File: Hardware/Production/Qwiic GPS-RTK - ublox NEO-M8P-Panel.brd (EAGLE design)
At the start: 95.5 x 94.2 mm, 406 parts, among them J11 PTH, J13 U.FL, J15 U.FL, J17 PTH, J20 U.FL, J3 PTH, J5 PTH, J9 U.FL, U1 NEO-M8P, U2 3.3V, U3 NEO-M8P, U4 3.3V, U5 NEO-M8P, U6 3.3V, U7 NEO-M8P, U8 3.3V

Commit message: Adding examples
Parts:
- removed JP52: (no value), SparkFun-Jumpers:SMT-JUMPER_2_NO_SILK
- removed JP53, JP54: (no value), SparkFun-Jumpers:SMT-JUMPER_2_NC_TRACE_SILK
- removed JP55: SPI, SparkFun-Connectors:1X06_NO_SILK
- added J21: (no value), SparkFun-Connectors:1X04_1MM_RA
- added J22: (no value), SparkFun-Connectors:USB-MICROB-PTH-MILL
- added J23: U.FL, SparkFun-Connectors:U.FL
- added J24: (no value), SparkFun-Connectors:1X07_NO_SILK
- added U$197, U$198: (no value), Labels:CS#-<]
- added U$199, U$200: (no value), Labels:MISO-(]-04
- added U$201, U$202: (no value), Labels:MOSI-(]-04
- added U$203, U$204: (no value), Labels:SCK-(]-04
- J1, J18: device SparkFun-Connectors:1X04_1MM_RA -> SparkFun-Connectors:1X07_NO_SILK
- J10: value (none) -> U.FL; device SparkFun-Connectors:1X04_1MM_RA -> SparkFun-Connectors:U.FL
- J11: value PTH -> (none); device SparkX:1X04_NO_SILK -> SparkFun-Connectors:1X07_NO_SILK
- J14: value (none) -> PTH; device SparkFun-Connectors:USB-MICROB-PTH-MILL -> SparkX:1X04_NO_SILK
- J15: value U.FL -> (none); device SparkFun-Connectors:U.FL -> SparkFun-Connectors:1X04_1MM_RA
- J16: device SparkFun-Connectors:1X04_1MM_RA -> SparkFun-Connectors:USB-MICROB-PTH-MILL
- J17: value PTH -> U.FL; device SparkX:1X04_NO_SILK -> SparkFun-Connectors:U.FL
- J19, J8: device SparkFun-Connectors:USB-MICROB-PTH-MILL -> SparkFun-Connectors:1X04_1MM_RA
- J20: value U.FL -> PTH; device SparkFun-Connectors:U.FL -> SparkX:1X04_NO_SILK
- J5: value PTH -> (none); device SparkX:1X04_NO_SILK -> SparkFun-Connectors:1X04_1MM_RA
- J7: value (none) -> PTH; device SparkFun-Connectors:1X04_1MM_RA -> SparkX:1X04_NO_SILK
- J9: value U.FL -> (none); device SparkFun-Connectors:U.FL -> SparkFun-Connectors:USB-MICROB-PTH-MILL
- JP11, JP38: value SPI -> FIDUCIALUFIDUCIAL; device SparkFun-Connectors:1X06_NO_SILK -> SparkFun:MICRO-FIDUCIAL
- JP13, JP29, JP30, JP46: value FIDUCIALUFIDUCIAL -> STAND-OFF; device SparkFun:MICRO-FIDUCIAL -> SparkFun:STAND-OFF
- JP16, JP32: value STAND-OFF -> (none); device SparkFun:STAND-OFF -> SparkFun-Jumpers:SMT-JUMPER_2_NO_SILK
- JP17, JP34: value SPI -> (none); device SparkFun-Connectors:1X06_NO_SILK -> SparkFun-Jumpers:SMT-JUMPER_2_NC_TRACE_SILK
- JP18: device SparkFun-Jumpers:SMT-JUMPER_2_NO_SILK -> SparkFun-Jumpers:SMT-JUMPER_2_NC_TRACE_SILK
- JP19: value (none) -> SPI; device SparkFun-Jumpers:SMT-JUMPER_2_NC_TRACE_SILK -> SparkFun-Connectors:1X06_NO_SILK
- JP20, JP36, JP37, JP45: value (none) -> STAND-OFF; device SparkFun-Jumpers:SMT-JUMPER_2_NC_TRACE_SILK -> SparkFun:STAND-OFF
- JP22: value SPI -> STAND-OFF; device SparkFun-Connectors:1X06_NO_SILK -> SparkFun:STAND-OFF
- JP23, JP24, JP39: value STAND-OFF -> FIDUCIALUFIDUCIAL; device SparkFun:STAND-OFF -> SparkFun:MICRO-FIDUCIAL
- JP25: value FIDUCIALUFIDUCIAL -> (none); device SparkFun:MICRO-FIDUCIAL -> SparkFun-Jumpers:SMT-JUMPER_3_2-NC_TRACE_SILK
- JP26, JP42: value FIDUCIALUFIDUCIAL -> (none); device SparkFun:MICRO-FIDUCIAL -> SparkFun-Jumpers:SMT-JUMPER_2_NC_TRACE_SILK
- JP27, JP44: value (none) -> FIDUCIALUFIDUCIAL; device SparkFun-Jumpers:SMT-JUMPER_3_2-NC_TRACE_SILK -> SparkFun:MICRO-FIDUCIAL
- JP28: value (none) -> FIDUCIALUFIDUCIAL; device SparkFun-Jumpers:SMT-JUMPER_2_NC_TRACE_SILK -> SparkFun:MICRO-FIDUCIAL
- JP33, JP48, JP49: value STAND-OFF -> (none); device SparkFun:STAND-OFF -> SparkFun-Jumpers:SMT-JUMPER_2_NC_TRACE_SILK
- JP35: value (none) -> SPI; device SparkFun-Jumpers:SMT-JUMPER_2_NO_SILK -> SparkFun-Connectors:1X06_NO_SILK
- JP40: value STAND-OFF -> (none); device SparkFun:STAND-OFF -> SparkFun-Jumpers:SMT-JUMPER_3_2-NC_TRACE_SILK
- JP47: value FIDUCIALUFIDUCIAL -> (none); device SparkFun:MICRO-FIDUCIAL -> SparkFun-Jumpers:SMT-JUMPER_2_NO_SILK
- R10, R25, R26, R40, R41, R55, R56, R9: value 33 -> 27
- U$100, U$151: device Labels:SCL-[) -> Labels:MOSI-(]-04
- U$101: device Labels:SDA-[) -> Labels:SCK-(]-04
- U$102: device Labels:SCL-[) -> Labels:SCK-(]-04
- U$103: device Labels:3V3-04 -> Labels:SDA-[)
- U$104: device Labels:3V3-04 -> Labels:SCL-[)
- U$105, U$154: device Labels:GND-04 -> Labels:SDA-[)
- U$106, U$155: device Labels:GND-04 -> Labels:SCL-[)
- U$107: device Labels:I_SUPER2_C-()-03 -> Labels:3V3-04
- U$108, U$158: device buzzard_labels (5):INT8 -> Labels:3V3-04
- U$109, U$51: device buzzard_labels (5):INT8 -> Labels:GND-04
- U$110: device buzzard_labels (5):U#BLOX3 -> Labels:GND-04
- U$111: device Labels:QWIIC-LOGO-MEDIUM -> Labels:I_SUPER2_C-()-03
- U$112, U$58: value SPARKX-LOGO3 -> (none); device SparkX:SPARKX-SMALL -> buzzard_labels (5):INT8
- U$113: value SPARKX-LOGO4 -> (none); device SparkX:SPARKX-MEDIUM -> buzzard_labels (5):INT8
- U$114: device buzzard_labels (7):#RST3 -> buzzard_labels (5):U#BLOX3
- U$115: device buzzard_labels (7):#RST3 -> Labels:QWIIC-LOGO-MEDIUM
- U$116: value (none) -> SPARKX-LOGO3; device buzzard_labels (7):#SAFE1 -> SparkX:SPARKX-SMALL
- U$117: value (none) -> SPARKX-LOGO4; device buzzard_labels (7):#SAFE1 -> SparkX:SPARKX-MEDIUM
- U$118, U$119: device buzzard_labels (7):PPS5 -> buzzard_labels (7):#RST3
- U$120: device buzzard_labels (33):PPS0 -> buzzard_labels (7):#SAFE1
- U$121: device buzzard_labels:FENCE2 -> buzzard_labels (7):#SAFE1
- U$122: device buzzard_labels:JP20 -> buzzard_labels (7):PPS5
- U$123: device buzzard_labels:RTK1 -> buzzard_labels (7):PPS5
- U$124: device buzzard_labels (1):FENCE0 -> buzzard_labels (33):PPS0
- U$125: device buzzard_labels (1):FENCE0 -> buzzard_labels:FENCE2
- U$126: device buzzard_labels (1):RTK1 -> buzzard_labels:JP20
- U$127: device buzzard_labels (1):RTK1 -> buzzard_labels:RTK1
- U$128, U$129: device Labels:MISO -> buzzard_labels (1):FENCE0
- U$130, U$131: device Labels:MOSI -> buzzard_labels (1):RTK1
- U$132, U$133, U$48, U$49: device Labels:SCK-[) -> Labels:3V3-04
- U$134, U$135, U$50: device Labels:CS#-[> -> Labels:GND-04
- U$136: device Labels:3V3-04 -> buzzard_labels (3):GPS#RTK0
- U$137: device Labels:3V3-04 -> buzzard_labels (5):JP10
- U$138: device Labels:GND-04 -> buzzard_labels (5):JP32
- U$139: device Labels:GND-04 -> buzzard_labels (6):DSEL0
- U$140: device buzzard_labels (3):GPS#RTK0 -> buzzard_labels (7):NEO#M8P3
- U$141: device buzzard_labels (5):JP10 -> buzzard_labels (8):GPS#RTK1
- U$142: device buzzard_labels (5):JP32 -> buzzard_labels (9):ANT0
- U$143: device buzzard_labels (6):DSEL0 -> Labels:PWR-()-03
- U$144: device buzzard_labels (7):NEO#M8P3 -> Labels:5V
- U$145: device buzzard_labels (8):GPS#RTK1 -> Labels:5V
- U$146: device buzzard_labels (9):ANT0 -> Labels:CS#-<]
- U$147: device Labels:PWR-()-03 -> Labels:CS#-<]
- U$148: device Labels:SDA-[) -> Labels:MISO-(]-04
- U$149: device Labels:SCL-[) -> Labels:MISO-(]-04
- U$150, U$99: device Labels:SDA-[) -> Labels:MOSI-(]-04
- U$152, U$153: device Labels:3V3-04 -> Labels:SCK-(]-04
- U$156: device Labels:I_SUPER2_C-()-03 -> Labels:SDA-[)
- U$157: device buzzard_labels (5):INT8 -> Labels:SCL-[)
- U$159: device buzzard_labels (5):U#BLOX3 -> Labels:3V3-04
- U$160: device Labels:QWIIC-LOGO-MEDIUM -> Labels:GND-04
- U$161: value SPARKX-LOGO3 -> (none); device SparkX:SPARKX-SMALL -> Labels:GND-04
- U$162: value SPARKX-LOGO4 -> (none); device SparkX:SPARKX-MEDIUM -> Labels:I_SUPER2_C-()-03
- U$163, U$164: device buzzard_labels (7):#RST3 -> buzzard_labels (5):INT8
- U$165: device buzzard_labels (7):#SAFE1 -> buzzard_labels (5):U#BLOX3
- U$166: device buzzard_labels (7):#SAFE1 -> Labels:QWIIC-LOGO-MEDIUM
- U$167: value (none) -> SPARKX-LOGO3; device buzzard_labels (7):PPS5 -> SparkX:SPARKX-SMALL
- U$168: value (none) -> SPARKX-LOGO4; device buzzard_labels (7):PPS5 -> SparkX:SPARKX-MEDIUM
- U$169: device buzzard_labels (33):PPS0 -> buzzard_labels (7):#RST3
- U$170: device buzzard_labels:FENCE2 -> buzzard_labels (7):#RST3
- U$171: device buzzard_labels:JP20 -> buzzard_labels (7):#SAFE1
- U$172: device buzzard_labels:RTK1 -> buzzard_labels (7):#SAFE1
- U$173, U$174: device buzzard_labels (1):FENCE0 -> buzzard_labels (7):PPS5
- U$175: device buzzard_labels (1):RTK1 -> buzzard_labels (33):PPS0
- U$176: device buzzard_labels (1):RTK1 -> buzzard_labels:FENCE2
- U$177: device Labels:MISO -> buzzard_labels:JP20
- U$178: device Labels:MISO -> buzzard_labels:RTK1
- U$179, U$180: device Labels:MOSI -> buzzard_labels (1):FENCE0
- U$181, U$182: device Labels:SCK-[) -> buzzard_labels (1):RTK1
- U$183, U$184: device Labels:CS#-[> -> Labels:3V3-04
- U$185, U$186: device Labels:3V3-04 -> Labels:GND-04
- U$187: device Labels:GND-04 -> buzzard_labels (3):GPS#RTK0
- U$188: device Labels:GND-04 -> buzzard_labels (5):JP10
- U$189: device buzzard_labels (3):GPS#RTK0 -> buzzard_labels (5):JP32
- U$19: device Labels:SDA-[) -> Labels:5V
- U$190: device buzzard_labels (5):JP10 -> buzzard_labels (6):DSEL0
- U$191: device buzzard_labels (5):JP32 -> buzzard_labels (7):NEO#M8P3
- U$192: device buzzard_labels (6):DSEL0 -> buzzard_labels (8):GPS#RTK1
- U$193: device buzzard_labels (7):NEO#M8P3 -> buzzard_labels (9):ANT0
- U$194: device buzzard_labels (8):GPS#RTK1 -> Labels:PWR-()-03
- U$195: device buzzard_labels (9):ANT0 -> Labels:5V
- U$196: device Labels:PWR-()-03 -> Labels:5V
- U$20: device Labels:SCL-[) -> Labels:5V
- U$23: device Labels:SDA-[) -> Labels:CS#-<]
- U$24: device Labels:SCL-[) -> Labels:CS#-<]
- U$26, U$33: device Labels:3V3-04 -> Labels:MISO-(]-04
- U$34, U$37: device Labels:GND-04 -> Labels:MOSI-(]-04
- U$38: device Labels:I_SUPER2_C-()-03 -> Labels:SCK-(]-04
- U$41: device buzzard_labels (5):INT8 -> Labels:SCK-(]-04
- U$42: device Labels:MISO -> Labels:SDA-[)
- U$45: device Labels:MISO -> Labels:SCL-[)
- U$46: device Labels:MOSI -> Labels:SDA-[)
- U$47: device Labels:MOSI -> Labels:SCL-[)
- U$56: device buzzard_labels (5):U#BLOX3 -> Labels:I_SUPER2_C-()-03
- U$57: device Labels:QWIIC-LOGO-MEDIUM -> buzzard_labels (5):INT8
- U$59: device Labels:CS#-[> -> buzzard_labels (5):U#BLOX3
- U$64: value SPARKX-LOGO4 -> (none); device SparkX:SPARKX-MEDIUM -> Labels:QWIIC-LOGO-MEDIUM
- U$65: value (none) -> SPARKX-LOGO3; device buzzard_labels (7):#RST3 -> SparkX:SPARKX-SMALL
- U$66: value (none) -> SPARKX-LOGO4; device buzzard_labels (7):#RST3 -> SparkX:SPARKX-MEDIUM
- U$67, U$68: device buzzard_labels (7):#SAFE1 -> buzzard_labels (7):#RST3
- U$69, U$70: device buzzard_labels (7):PPS5 -> buzzard_labels (7):#SAFE1
- U$71: device buzzard_labels (33):PPS0 -> buzzard_labels (7):PPS5
- U$72: device buzzard_labels:FENCE2 -> buzzard_labels (7):PPS5
- U$73: device buzzard_labels:JP20 -> buzzard_labels (33):PPS0
- U$74: device buzzard_labels:RTK1 -> buzzard_labels:FENCE2
- U$75: device buzzard_labels (1):FENCE0 -> buzzard_labels:JP20
- U$76: device buzzard_labels (1):FENCE0 -> buzzard_labels:RTK1
- U$77, U$78: device buzzard_labels (1):RTK1 -> buzzard_labels (1):FENCE0
- U$79, U$80: device Labels:MISO -> buzzard_labels (1):RTK1
- U$81, U$82: device Labels:MOSI -> Labels:3V3-04
- U$83, U$84: device Labels:SCK-[) -> Labels:GND-04
- U$85: device Labels:CS#-[> -> buzzard_labels (3):GPS#RTK0
- U$86: device Labels:CS#-[> -> buzzard_labels (5):JP10
- U$87: device Labels:3V3-04 -> buzzard_labels (5):JP32
- U$88: device Labels:3V3-04 -> buzzard_labels (6):DSEL0
- U$89: device Labels:GND-04 -> buzzard_labels (7):NEO#M8P3
- U$90: device Labels:GND-04 -> buzzard_labels (8):GPS#RTK1
- U$91: device buzzard_labels (3):GPS#RTK0 -> buzzard_labels (9):ANT0
- U$92: device buzzard_labels (5):JP10 -> Labels:PWR-()-03
- U$93: device buzzard_labels (5):JP32 -> Labels:5V
- U$94: device buzzard_labels (6):DSEL0 -> Labels:5V
- U$95: device buzzard_labels (7):NEO#M8P3 -> Labels:CS#-<]
- U$96: device buzzard_labels (8):GPS#RTK1 -> Labels:CS#-<]
- U$97: device buzzard_labels (9):ANT0 -> Labels:MISO-(]-04
- U$98: device Labels:PWR-()-03 -> Labels:MISO-(]-04
- moved JP20 95.5 mm to (2.54, 66.5), flipped to the top
- moved J10 73.9 mm to (72.5, 22.4), turned to 180 degrees
- moved JP22 69.8 mm to (38.1, 66.5), turned to 0 degrees
- moved JP11 67.2 mm to (81.2, 0.64), flipped to the bottom
- moved J18 59.6 mm to (19.1, 67.8), turned to 0 degrees
- moved JP38 59.6 mm to (81.2, 36.7), turned to 0 degrees
- moved U$20 57.5 mm to (21.6, 27.7), flipped to the bottom
- moved U$19 55.3 mm to (21.6, 27.7)
- moved U$24 53.2 mm to (26.7, 27.9)
- moved U$47 52.9 mm to (72.9, 1.65), flipped to the bottom, turned to 90 degrees
- moved U$23 51.0 mm to (26.7, 27.9), flipped to the top
- moved U$46 50.8 mm to (70.4, 1.65), turned to 90 degrees
- moved U$45 50.8 mm to (72.9, 1.65), flipped to the top, turned to 90 degrees
- moved JP12 50.6 mm to (41.8, 32.4)
- moved JP43 50.6 mm to (81.2, 36.7), flipped to the bottom
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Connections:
- net !RESET1: now also JP19.3; no longer JP22.3
- net !RESET2: now also JP35.3; no longer JP38.3
- net !RESET3: now also JP50.3; no longer JP55.3
- net !SAFE1: now also JP19.2; no longer JP22.2
- net !SAFE2: now also JP35.2; no longer JP38.2
- net !SAFE3: now also JP50.2; no longer JP55.2
- net 3.3V: now also J1.3; no longer JP11.2
- net 3.3V1: now also J11.3, J8.2; no longer J1.2, JP17.2
- net 3.3V2: now also J14.2, J15.2, J18.3, JP25.2; no longer J10.2, J11.2, JP27.2, JP34.2
- net 3.3V3: now also J19.2, J20.2, J21.2, J24.3, JP40.2; no longer J16.2, J17.2, J18.2, JP44.2, JP50.2
- net 5V: now also J1.2
- net 5V1: now also J11.2, J9.VBUS; no longer J8.VBUS
- net 5V2: now also J16.VBUS, J18.2; no longer J14.VBUS
- net 5V3: now also J22.VBUS, J24.2; no longer J19.VBUS
- net D_SEL1: now also JP16.2; no longer JP18.2
- net D_SEL2: now also JP32.2; no longer JP35.2
- net D_SEL3: now also JP47.2; no longer JP52.2
- net FENCE_STAT1: now also JP18.2, JP19.6; no longer JP20.2, JP22.6
- net FENCE_STAT2: now also JP34.2, JP35.6; no longer JP37.2, JP38.6
- net FENCE_STAT3: now also JP49.2, JP50.6; no longer JP54.2, JP55.6
- net GND: now also J1.1; no longer JP11.1
- net GND1: now also J10.1, J10.2, J11.1, J8.1, J9.GND, JP16.1; no longer J1.1, J8.GND, J9.1, J9.2, JP17.1, JP18.1
- net GND2: now also J14.1, J16.GND, J17.1, J17.2, J18.1, JP32.1; no longer J10.1, J11.1, J14.GND, J15.2, JP34.1, JP35.1
- net GND3: now also J19.1, J21.1, J22.GND, J23.1, J23.2, J24.1, JP47.1; no longer J16.1, J17.1, J18.1, J19.GND, J20.2, JP50.1, JP52.1
- net GPS_ANT2: now also J10.FEED; no longer J9.FEED
- net GPS_ANT3: now also J17.FEED; no longer J15.FEED
- net GPS_ANT4: now also J23.FEED; no longer J20.FEED
- net INT1: now also JP19.1; no longer JP22.1
- net INT2: now also JP35.1; no longer JP38.1
- net INT3: now also JP50.1; no longer JP55.1
- net N$23: now also JP17.1; no longer JP19.1
- net N$25: now also JP18.1; no longer JP20.1
- net N$27: now also JP25.1; no longer JP27.1
- net N$28: now also JP25.3; no longer JP27.3
- net N$30: now also JP26.1; no longer JP28.1
- net N$36: now also JP33.1; no longer JP36.1
- net N$38: now also JP34.1; no longer JP37.1
- net N$40: now also JP40.1; no longer JP44.1
- net N$41: now also JP40.3; no longer JP44.3
- net N$43: now also JP42.1; no longer JP45.1
- net N$49: now also JP48.1; no longer JP53.1
- net N$51: now also JP49.1; no longer JP54.1
- net PPS1: now also JP19.4; no longer JP22.4
- net PPS2: now also JP26.2, JP35.4; no longer JP28.2, JP38.4
- net PPS3: now also JP42.2, JP50.4; no longer JP45.2, JP55.4
- net RTK_STAT1: now also JP17.2, JP19.5; no longer JP19.2, JP22.5
- net RTK_STAT2: now also JP33.2, JP35.5; no longer JP36.2, JP38.5
- net RTK_STAT3: now also JP48.2, JP50.5; no longer JP53.2, JP55.5
- net RXI/MOSI: now also J1.5; no longer JP11.4
- net RXI/MOSI1: now also J11.5; no longer JP17.4
- net RXI/MOSI2: now also J18.5; no longer JP34.4
- net RXI/MOSI3: now also J24.5; no longer JP50.4
- net SCL/SCK: now also J1.7; no longer JP11.6
- net SCL/SCK1: now also J11.7, J8.4; no longer J1.4, JP17.6
- net SCL/SCK2: now also J14.4, J15.4, J18.7; no longer J10.4, J11.4, JP34.6
- net SCL/SCK3: now also J19.4, J20.4, J21.4, J24.7; no longer J16.4, J17.4, J18.4, JP50.6
- net SDA/!CS: now also J1.4; no longer JP11.3
- net SDA/!CS1: now also J11.4, J8.3; no longer J1.3, JP17.3
- net SDA/!CS2: now also J14.3, J15.3, J18.4; no longer J10.3, J11.3, JP34.3
- net SDA/!CS3: now also J19.3, J20.3, J21.3, J24.4; no longer J16.3, J17.3, J18.3, JP50.3
- net SHLD1: now also J9.SHIELD, J9.SHIELD10, J9.SHIELD2, J9.SHIELD3, J9.SHIELD4, J9.SHIELD5, J9.SHIELD6, J9.SHIELD7, J9.SHIELD8, J9.SHIELD9; no longer J8.SHIELD, J8.SHIELD10, J8.SHIELD2, J8.SHIELD3, J8.SHIELD4, J8.SHIELD5, J8.SHIELD6, J8.SHIELD7, J8.SHIELD8, J8.SHIELD9
- net SHLD2: now also J16.SHIELD, J16.SHIELD10, J16.SHIELD2, J16.SHIELD3, J16.SHIELD4, J16.SHIELD5, J16.SHIELD6, J16.SHIELD7, J16.SHIELD8, J16.SHIELD9; no longer J14.SHIELD, J14.SHIELD10, J14.SHIELD2, J14.SHIELD3, J14.SHIELD4, J14.SHIELD5, J14.SHIELD6, J14.SHIELD7, J14.SHIELD8, J14.SHIELD9
- net SHLD3: now also J22.SHIELD, J22.SHIELD10, J22.SHIELD2, J22.SHIELD3, J22.SHIELD4, J22.SHIELD5, J22.SHIELD6, J22.SHIELD7, J22.SHIELD8, J22.SHIELD9; no longer J19.SHIELD, J19.SHIELD10, J19.SHIELD2, J19.SHIELD3, J19.SHIELD4, J19.SHIELD5, J19.SHIELD6, J19.SHIELD7, J19.SHIELD8, J19.SHIELD9
- net TXO/MISO: now also J1.6; no longer JP11.5
- net TXO/MISO1: now also J11.6; no longer JP17.5
- net TXO/MISO2: now also J18.6; no longer JP34.5
- net TXO/MISO3: now also J24.6; no longer JP50.5
- net USB_D+1: now also J9.D+; no longer J8.D+
- net USB_D+2: now also J16.D+; no longer J14.D+
- net USB_D+3: now also J22.D+; no longer J19.D+
- net USB_D-1: now also J9.D-; no longer J8.D-
- net USB_D-2: now also J16.D-; no longer J14.D-
- net USB_D-3: now also J22.D-; no longer J19.D-
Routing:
- net 5V3: track 21.3 -> 53.6 mm
- net 5V: track 21.3 -> 53.6 mm
- net 5V2: track 21.3 -> 53.6 mm
- net 5V1: track 21.3 -> 53.6 mm
- net N$33: track 25.6 -> 55.8 mm
- net N$46: track 25.6 -> 55.8 mm
- net N$11: track 25.6 -> 55.8 mm
- net N$20: track 25.6 -> 55.8 mm
- net N$34: track 24.4 -> 52.4 mm
- net N$12: track 24.4 -> 52.4 mm
- net N$47: track 24.4 -> 52.4 mm
- net N$21: track 24.4 -> 52.4 mm
- net INT2: track 15.5 -> 24.0 mm
- net INT: track 15.5 -> 24.0 mm
- net INT1: track 15.5 -> 24.0 mm
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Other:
- board text added: "x02"
- board text removed: "x01"

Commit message: Modifications for reds.
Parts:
- removed E$4: (no value), SparkFun-Aesthetics:FIDUCIAL-1X2
- removed E$5, E$6: (no value), SparkFun-Retired:FIDUCIAL-1.5X3
- removed U$201, U$202: (no value), Labels:MOSI-(]-04
- removed U$203, U$204: (no value), Labels:SCK-(]-04
- added LOGO5, LOGO7: OSHW-LOGOMINI, SparkFun-Aesthetics:OSHW-LOGO-MINI
- added LOGO6, LOGO8: SFE_LOGO_NAME_FLAME.1_INCH, SparkFun-Aesthetics:SFE_LOGO_NAME_FLAME_.1
- D1, D11, D16, D6: value BLUE -> Yellow
- E$3: device SparkFun-Aesthetics:FIDUCIAL-1X2 -> SparkFun-Retired:FIDUCIAL-1.5X3
- JP10, JP26, JP42: device SparkFun-Jumpers:SMT-JUMPER_2_NC_TRACE_SILK -> SparkFun-Jumpers:SMT-JUMPER_3_2-NC_TRACE_SILK
- JP11, JP27, JP43: value FIDUCIALUFIDUCIAL -> (none); device SparkFun:MICRO-FIDUCIAL -> SparkFun-Jumpers:SMT-JUMPER_2_NC_TRACE_SILK
- JP13, JP29, JP45: value STAND-OFF -> FIDUCIALUFIDUCIAL; device SparkFun:STAND-OFF -> SparkFun:MICRO-FIDUCIAL
- JP15: value SPI -> (none)
- JP16, JP32, JP47: value (none) -> STAND-OFF; device SparkFun-Jumpers:SMT-JUMPER_2_NO_SILK -> SparkFun:STAND-OFF
- JP17, JP33, JP48: device SparkFun-Jumpers:SMT-JUMPER_2_NC_TRACE_SILK -> SparkFun-Jumpers:SMT-JUMPER_2_NO_SILK
- JP19, JP35, JP50: value SPI -> (none); device SparkFun-Connectors:1X06_NO_SILK -> SparkFun-Jumpers:SMT-JUMPER_2_NC_TRACE_SILK
- JP20, JP36: value STAND-OFF -> (none); device SparkFun:STAND-OFF -> SparkFun-Connectors:1X06_NO_SILK
- JP23, JP38, JP7: value FIDUCIALUFIDUCIAL -> STAND-OFF; device SparkFun:MICRO-FIDUCIAL -> SparkFun:STAND-OFF
- JP25, JP40, JP9: value (none) -> FIDUCIALUFIDUCIAL; device SparkFun-Jumpers:SMT-JUMPER_3_2-NC_TRACE_SILK -> SparkFun:MICRO-FIDUCIAL
- JP5: value STAND-OFF -> (none); device SparkFun:STAND-OFF -> SparkFun-Jumpers:SMT-JUMPER_3_2-NC_TRACE_SILK
- JP51: device SparkFun-Jumpers:SMT-JUMPER_3_2-NC_TRACE_SILK -> SparkFun-Connectors:1X06_NO_SILK
- LOGO2, LOGO4: value OSHW-LOGOMINI -> SFE_LOGO_NAME_FLAME.1_INCH; device SparkFun-Aesthetics:OSHW-LOGO-MINI -> SparkFun-Aesthetics:SFE_LOGO_NAME_FLAME_.1
- U$100, U$150, U$37: device Labels:MOSI-(]-04 -> buzzard_labels (36):TX#MISO1
- U$101, U$153: device Labels:SCK-(]-04 -> Labels:SDA-[)
- U$102, U$152: device Labels:SCK-(]-04 -> Labels:SCL-[)
- U$105, U$156: device Labels:SDA-[) -> Labels:3V3-04
- U$106, U$155, U$47: device Labels:SCL-[) -> Labels:3V3-04
- U$107, U$108, U$158, U$49, U$81: device Labels:3V3-04 -> Labels:GND-04
- U$109, U$51: device Labels:GND-04 -> Labels:I_SUPER2_C-()-03
- U$110, U$160, U$161: device Labels:GND-04 -> buzzard_labels (5):INT8
- U$111, U$56: device Labels:I_SUPER2_C-()-03 -> buzzard_labels (5):INT8
- U$112, U$58: device buzzard_labels (5):INT8 -> buzzard_labels (5):U#BLOX3
- U$113, U$163: device buzzard_labels (5):INT8 -> Labels:QWIIC-LOGO-MEDIUM
- U$114, U$165: device buzzard_labels (5):U#BLOX3 -> buzzard_labels (7):#RST3
- U$115, U$64: device Labels:QWIIC-LOGO-MEDIUM -> buzzard_labels (7):#RST3
- U$116, U$167: value SPARKX-LOGO3 -> (none); device SparkX:SPARKX-SMALL -> buzzard_labels (7):#SAFE1
- U$117, U$66: value SPARKX-LOGO4 -> (none); device SparkX:SPARKX-MEDIUM -> buzzard_labels (7):#SAFE1
- U$118, U$119, U$169, U$68: device buzzard_labels (7):#RST3 -> buzzard_labels (7):PPS5
- U$120, U$70: device buzzard_labels (7):#SAFE1 -> buzzard_labels (33):PPS0
- U$121, U$171: device buzzard_labels (7):#SAFE1 -> buzzard_labels:FENCE2
- U$122, U$72: device buzzard_labels (7):PPS5 -> buzzard_labels:JP20
- U$123, U$173: device buzzard_labels (7):PPS5 -> buzzard_labels:RTK1
- U$124, U$175: device buzzard_labels (33):PPS0 -> buzzard_labels (1):FENCE0
- U$125, U$74: device buzzard_labels:FENCE2 -> buzzard_labels (1):FENCE0
- U$126, U$177: device buzzard_labels:JP20 -> buzzard_labels (1):RTK1
- U$127, U$76: device buzzard_labels:RTK1 -> buzzard_labels (1):RTK1
- U$128, U$129, U$179, U$78: device buzzard_labels (1):FENCE0 -> Labels:3V3-04
- U$130, U$131, U$181, U$80: device buzzard_labels (1):RTK1 -> Labels:GND-04
- U$132, U$82: device Labels:3V3-04 -> buzzard_labels (3):GPS#RTK0
- U$133, U$183: device Labels:3V3-04 -> buzzard_labels (5):JP10
- U$134, U$84: device Labels:GND-04 -> buzzard_labels (5):JP32
- U$135, U$185: device Labels:GND-04 -> buzzard_labels (6):DSEL0
- U$136: device buzzard_labels (3):GPS#RTK0 -> buzzard_labels (7):NEO#M8P3
- U$137: device buzzard_labels (5):JP10 -> buzzard_labels (8):GPS#RTK1
- U$138: device buzzard_labels (5):JP32 -> buzzard_labels (9):ANT0
- U$139: device buzzard_labels (6):DSEL0 -> Labels:PWR-()-03
- U$140, U$191: device buzzard_labels (7):NEO#M8P3 -> Labels:5V
- U$141, U$90: device buzzard_labels (8):GPS#RTK1 -> Labels:5V
- U$142, U$193: device buzzard_labels (9):ANT0 -> Labels:CS#-<]
- U$143, U$92: device Labels:PWR-()-03 -> Labels:CS#-<]
- U$144, U$145, U$195, U$94: device Labels:5V -> Labels:SCK-(]-04
- U$146, U$96: device Labels:CS#-<] -> SparkFun-Aesthetics:SFE_LOGO_FLAME_.1
- U$147, U$197: device Labels:CS#-<] -> buzzard_labels (36):RX#MOSI2
- U$148, U$98: device Labels:MISO-(]-04 -> buzzard_labels (36):RX#MOSI3
- U$149, U$199: device Labels:MISO-(]-04 -> buzzard_labels (36):TX#MISO0
- U$151: device Labels:MOSI-(]-04 -> Labels:SDA-[)
- U$154, U$42, U$46: device Labels:SDA-[) -> Labels:SCL-[)
- U$157: device Labels:SCL-[) -> Labels:GND-04
- U$159: device Labels:3V3-04 -> Labels:I_SUPER2_C-()-03
- U$162: device Labels:I_SUPER2_C-()-03 -> buzzard_labels (5):U#BLOX3
- U$164: device buzzard_labels (5):INT8 -> buzzard_labels (7):#RST3
- U$166: device Labels:QWIIC-LOGO-MEDIUM -> buzzard_labels (7):#SAFE1
- U$168: value SPARKX-LOGO4 -> (none); device SparkX:SPARKX-MEDIUM -> buzzard_labels (7):PPS5
- U$170: device buzzard_labels (7):#RST3 -> buzzard_labels (33):PPS0
- U$172: device buzzard_labels (7):#SAFE1 -> buzzard_labels:JP20
- U$174: device buzzard_labels (7):PPS5 -> buzzard_labels (1):FENCE0
- U$176: device buzzard_labels:FENCE2 -> buzzard_labels (1):RTK1
- U$178: device buzzard_labels:RTK1 -> Labels:3V3-04
- U$180: device buzzard_labels (1):FENCE0 -> Labels:GND-04
- U$182: device buzzard_labels (1):RTK1 -> buzzard_labels (3):GPS#RTK0
- U$184: device Labels:3V3-04 -> buzzard_labels (5):JP32
- U$186: device Labels:GND-04 -> buzzard_labels (7):NEO#M8P3
- U$187: device buzzard_labels (3):GPS#RTK0 -> buzzard_labels (8):GPS#RTK1
- U$188: device buzzard_labels (5):JP10 -> buzzard_labels (9):ANT0
- U$189: device buzzard_labels (5):JP32 -> Labels:PWR-()-03
- U$190: device buzzard_labels (6):DSEL0 -> Labels:5V
- U$192: device buzzard_labels (8):GPS#RTK1 -> Labels:CS#-<]
- U$194: device Labels:PWR-()-03 -> Labels:SCK-(]-04
- U$196: device Labels:5V -> SparkFun-Aesthetics:SFE_LOGO_FLAME_.1
- U$198: device Labels:CS#-<] -> buzzard_labels (36):RX#MOSI3
- U$2: value SPARKX-LOGO4 -> (none); device SparkX:SPARKX-MEDIUM -> Labels:SDA-[)
- U$200: device Labels:MISO-(]-04 -> buzzard_labels (36):TX#MISO1
- U$26, U$97: device Labels:MISO-(]-04 -> buzzard_labels (36):RX#MOSI2
- U$31: value SPARKX-LOGO3 -> (none); device SparkX:SPARKX-SMALL -> buzzard_labels (36):RX#MOSI3
- U$33: device Labels:MISO-(]-04 -> SparkFun-Aesthetics:SFE_LOGO_FLAME_.1
- U$34, U$99: device Labels:MOSI-(]-04 -> buzzard_labels (36):TX#MISO0
- U$45: device Labels:SCL-[) -> Labels:SDA-[)
- U$59: device buzzard_labels (5):U#BLOX3 -> Labels:QWIIC-LOGO-MEDIUM
- U$65: value SPARKX-LOGO3 -> (none); device SparkX:SPARKX-SMALL -> buzzard_labels (7):#RST3
- U$67: device buzzard_labels (7):#RST3 -> buzzard_labels (7):#SAFE1
- U$69: device buzzard_labels (7):#SAFE1 -> buzzard_labels (7):PPS5
- U$71: device buzzard_labels (7):PPS5 -> buzzard_labels:FENCE2
- U$73: device buzzard_labels (33):PPS0 -> buzzard_labels:RTK1
- U$75: device buzzard_labels:JP20 -> buzzard_labels (1):FENCE0
- U$77: device buzzard_labels (1):FENCE0 -> buzzard_labels (1):RTK1
- U$79: device buzzard_labels (1):RTK1 -> Labels:3V3-04
- U$83: device Labels:GND-04 -> buzzard_labels (5):JP10
- U$85: device buzzard_labels (3):GPS#RTK0 -> buzzard_labels (6):DSEL0
- U$86: device buzzard_labels (5):JP10 -> buzzard_labels (7):NEO#M8P3
- U$87: device buzzard_labels (5):JP32 -> buzzard_labels (8):GPS#RTK1
- U$88: device buzzard_labels (6):DSEL0 -> buzzard_labels (9):ANT0
- U$89: device buzzard_labels (7):NEO#M8P3 -> Labels:PWR-()-03
- U$91: device buzzard_labels (9):ANT0 -> Labels:5V
- U$93: device Labels:5V -> Labels:CS#-<]
- U$95: device Labels:CS#-<] -> Labels:SCK-(]-04
- moved E$3 101.9 mm to (6.86, -2.10)
- moved JP20 88.8 mm to (62.7, 1.27), turned to 180 degrees
- moved E$2 68.3 mm to (74.9, 68.6), flipped to the top
- moved JP51 58.9 mm to (62.7, 34.8)
- moved LOGO3 54.7 mm to (43.7, 26.7)
- moved U$2 53.9 mm to (70.4, 1.65), flipped to the top, turned to 90 degrees
- moved JP24 52.2 mm to (40.0, 34.2)
- moved JP28 52.2 mm to (40.0, 34.2)
- moved JP39 52.2 mm to (81.2, 34.2)
- moved JP44 52.2 mm to (81.2, 34.2)
- moved JP12 50.6 mm to (81.2, 0.64)
- moved JP8 50.6 mm to (81.2, 0.64)
- moved LOGO4 49.4 mm to (67.4, 19.4)
- moved U$151 49.2 mm to (70.4, 35.2), flipped to the top
- moved U$152 47.6 mm to (72.9, 35.2)
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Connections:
- net !RESET1: now also JP20.3; no longer JP19.3
- net !RESET2: now also JP36.3; no longer JP35.3
- net !RESET3: now also JP51.3; no longer JP50.3
- net !SAFE1: now also JP20.2; no longer JP19.2
- net !SAFE2: now also JP36.2; no longer JP35.2
- net !SAFE3: now also JP51.2; no longer JP50.2
- net 3.3V: now also JP5.2; no longer JP51.2
- net 3.3V1: now also JP10.2; no longer JP9.2
- net 3.3V2: now also JP26.2; no longer JP25.2
- net 3.3V3: now also JP42.2; no longer JP40.2
- net D_SEL1: now also JP17.2; no longer JP16.2
- net D_SEL2: now also JP33.2; no longer JP32.2
- net D_SEL3: now also JP48.2; no longer JP47.2
- net FENCE_STAT1: now also JP19.2, JP20.6; no longer JP18.2, JP19.6
- net FENCE_STAT2: now also JP35.2, JP36.6; no longer JP34.2, JP35.6
- net FENCE_STAT3: now also JP50.2, JP51.6; no longer JP49.2, JP50.6
- net GND1: now also JP17.1; no longer JP16.1
- net GND2: now also JP33.1; no longer JP32.1
- net GND3: now also JP48.1; no longer JP47.1
- net INT1: now also JP20.1; no longer JP19.1
- net INT2: now also JP36.1; no longer JP35.1
- net INT3: now also JP51.1; no longer JP50.1
- net N$14: now also JP10.1; no longer JP9.1
- net N$15: now also JP10.3; no longer JP9.3
- net N$17: now also JP11.1; no longer JP10.1
- net N$23: now also JP18.1; no longer JP17.1
- net N$25: now also JP19.1; no longer JP18.1
- net N$27: now also JP26.1; no longer JP25.1
- net N$28: now also JP26.3; no longer JP25.3
- net N$30: now also JP27.1; no longer JP26.1
- net N$36: now also JP34.1; no longer JP33.1
- net N$38: now also JP35.1; no longer JP34.1
- net N$40: now also JP42.1; no longer JP40.1
- net N$41: now also JP42.3; no longer JP40.3
- net N$43: now also JP43.1; no longer JP42.1
- net N$49: now also JP49.1; no longer JP48.1
- net N$5: now also JP5.1; no longer JP51.1
- net N$51: now also JP50.1; no longer JP49.1
- net N$8: now also JP5.3; no longer JP51.3
- net PPS1: now also JP11.2, JP20.4; no longer JP10.2, JP19.4
- net PPS2: now also JP27.2, JP36.4; no longer JP26.2, JP35.4
- net PPS3: now also JP43.2, JP51.4; no longer JP42.2, JP50.4
- net RTK_STAT1: now also JP18.2, JP20.5; no longer JP17.2, JP19.5
- net RTK_STAT2: now also JP34.2, JP36.5; no longer JP33.2, JP35.5
- net RTK_STAT3: now also JP49.2, JP51.5; no longer JP48.2, JP50.5
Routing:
- net PPS2: track 30.6 -> 38.9 mm, vias 2 -> 5
- net PPS: track 30.6 -> 38.9 mm, vias 2 -> 5
- net PPS3: track 30.6 -> 38.9 mm, vias 2 -> 5
- net PPS1: track 30.6 -> 38.9 mm, vias 2 -> 5
- net GND2: track 8.19 -> 5.71 mm
- net GND: track 8.19 -> 5.71 mm
- net GND1: track 8.19 -> 5.71 mm
- net GND3: track 8.19 -> 5.71 mm
- net 3.3V: track 120.0 -> 118.9 mm
- net 3.3V1: track 120.0 -> 118.9 mm
- net 3.3V3: track 120.0 -> 118.9 mm
- net 3.3V2: track 120.0 -> 118.9 mm
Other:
- board size 95.5 x 94.2 mm -> 101.9 x 86.6 mm
- board text added: "v10"
- board text removed: "Route Out"
- board text removed: "x02"

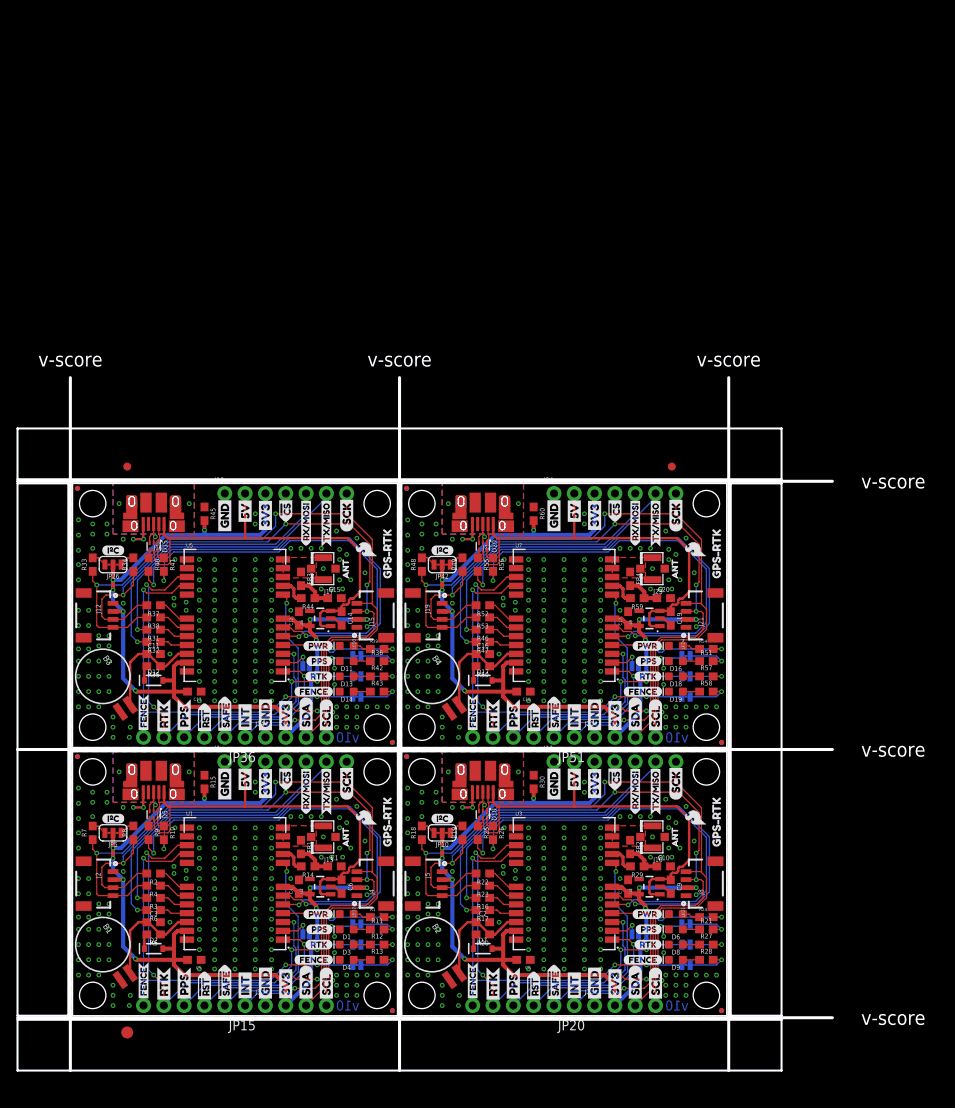
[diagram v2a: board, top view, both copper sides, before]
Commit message: Panel update, now with route outs!
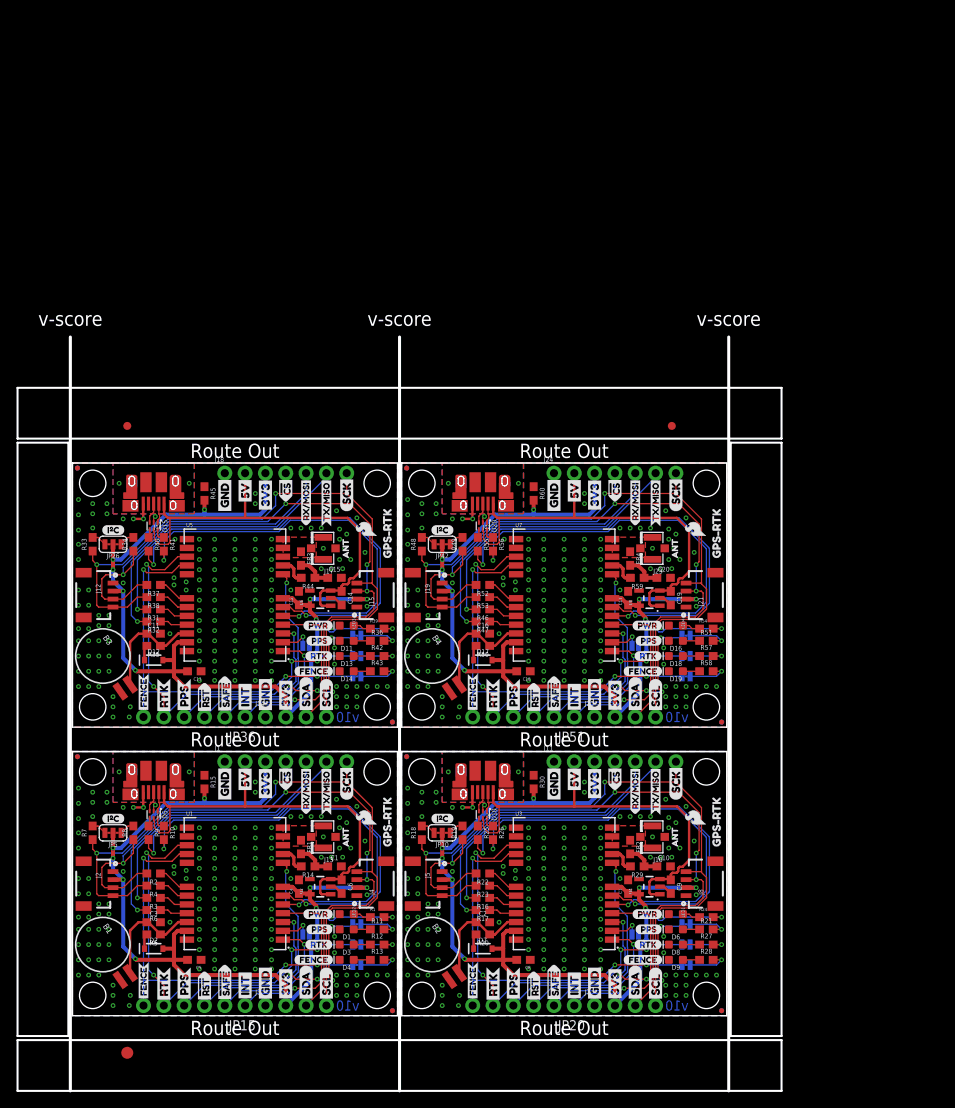
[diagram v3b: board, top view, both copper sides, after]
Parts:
- moved E$1 5.08 mm to (6.86, 73.7)
- moved E$2 5.08 mm to (74.9, 73.7)
- moved C12 2.54 mm to (28.3, 52.2)
- moved C14 2.54 mm to (33.7, 52.2)
- moved C17 2.54 mm to (69.5, 52.2)
- moved C19 2.54 mm to (74.8, 52.2)
- moved D12 2.54 mm to (10.2, 44.5)
- moved D17 2.54 mm to (51.3, 44.5)
- moved J12 2.54 mm to (5.08, 52.6)
- moved J15 2.54 mm to (35.6, 52.6)
- moved J19 2.54 mm to (46.2, 52.6)
- moved J21 2.54 mm to (76.7, 52.6)
- moved JP22 2.54 mm to (2.54, 66.5)
- moved JP23 2.54 mm to (38.1, 66.5)
- moved JP24 2.54 mm to (40.0, 36.7)
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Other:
- board size 101.9 x 86.6 mm -> 95.5 x 94.2 mm
- board text added: "Route Out"
